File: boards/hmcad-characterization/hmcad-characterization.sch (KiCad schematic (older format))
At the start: 46 parts, among them J1 BARREL, J10 SMA, J11 SMA, J12 CONN_INTEGRALSTICK_FPGA_HOST, J2 SMA, J3 SMA, J4 SMA, J5 SMA, J6 SMA, J7 SMA, J8 SMA, J9 SMA, U1 ASG2-D-X-A-1000.000MHZ, U2 SIT9122AI-2D3-33E625.000000T, U3 PI6C59S6005, U4 LT3042, U5 HMCAD1520

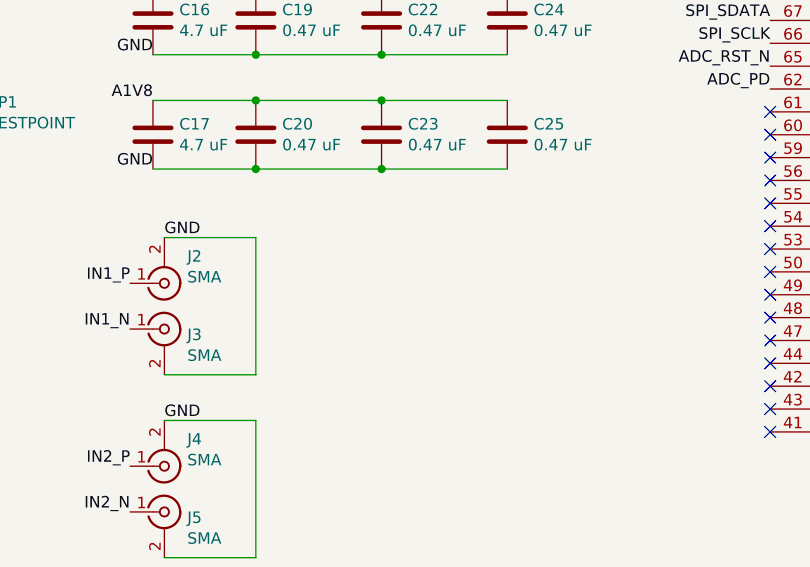
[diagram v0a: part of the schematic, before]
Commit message: finished schematic review on hmcad-characterization, ready to start layout
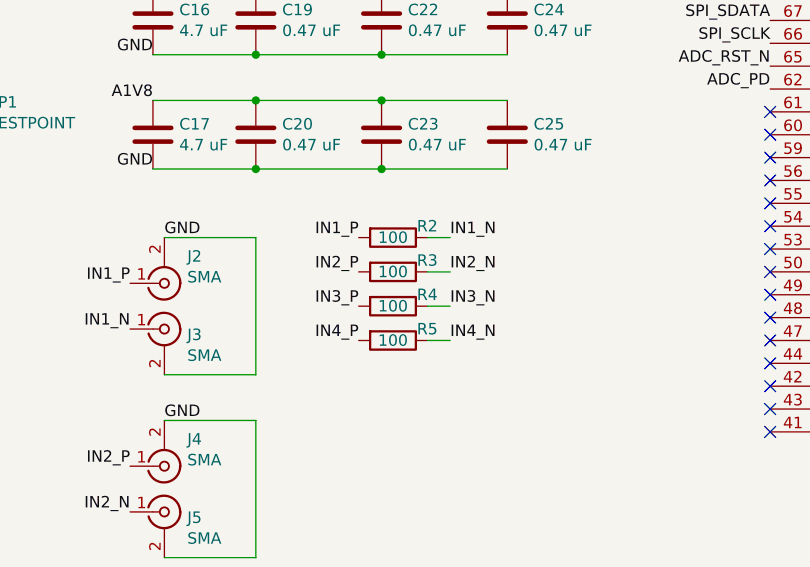
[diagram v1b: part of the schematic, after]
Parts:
- added R2, R3, R4, R5: 100, azonenberg_pcb:EIA_0402_RES_NOSILK, symbol device:R
- C1, C11, C12, C13, C14, C15, C18, C19, C2, C20, C21, C22, C23, C24, C25, C4, C5, C6, C7, C8, C9: footprint (none) -> azonenberg_pcb:EIA_0402_CAP_NOSILK
- C10, C16, C17, C3: footprint (none) -> azonenberg_pcb:EIA_0603_CAP_NOSILK
- F1, FB1: footprint (none) -> azonenberg_pcb:EIA_0603_INDUCTOR_NOSILK
- J1: footprint (none) -> azonenberg_pcb:CONN_CUI_PJ-058BH_HIPWR_BARREL_NOSLOT
- J10, J11, J2, J3, J4, J5, J6, J7, J8, J9: footprint (none) -> azonenberg_pcb:CONN_SMA_EDGE_SAMTEC_SMA_J_P_H_ST_EM1
- J12: footprint (none) -> azonenberg_pcb:CONN_SAMTEC_QSH-060-01-L-D-A
- R1: footprint (none) -> azonenberg_pcb:EIA_0402_RES_NOSILK
- TP1: footprint (none) -> azonenberg_pcb:TESTPOINT_SMT_0.5MM
- U1: footprint (none) -> azonenberg_pcb:OSCILLATOR_LVDS_2.5x2.0
- U2: footprint (none) -> azonenberg_pcb:OSCILLATOR_LVDS_7.0x5.0
- U3: footprint (none) -> azonenberg_pcb:QFN_24_0.5MM_4x4MM
- U4: footprint (none) -> azonenberg_pcb:DFN_10_0.5MM_3x3MM
- U5: footprint (none) -> azonenberg_pcb:QFN_48_0.5MM_7x7MM
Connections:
- net IN1_N: now also R2.1
- net IN1_P: now also R2.2
- net IN2_N: now also R3.1
- net IN2_P: now also R3.2
- net IN3_N: now also R4.1
- net IN3_P: now also R4.2
- net IN4_N: now also R5.1
- net IN4_P: now also R5.2

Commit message: Continued layout on ADC test board. Fixed a bunch of plane crossings.
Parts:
- added C26, C27: 4.7 uF, azonenberg_pcb:EIA_0603_CAP_NOSILK, symbol device:C
- added C28: 0.47 uF, azonenberg_pcb:EIA_0402_CAP_NOSILK, symbol device:C
- added U6: LT3042, azonenberg_pcb:DFN_10_0.5MM_3x3MM, symbol power-azonenberg:LT3042
- R1: value 33K 1% -> 9.09K 0.1%
- U1, U2: symbol osc-azonenberg:OSC_LVDS -> osc-azonenberg:OSC_LVDS_NOPAD
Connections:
- net 1V8: now also C28.1
- net 3V3: now also C28.2; no longer U4.6 (PGFB)
- net A1V8: now also C27.2, U6.10 (OUT), U6.9 (OUTS)
- net ADC_PD: now also J12.68 (IO_1V8); no longer J12.62 (IO_1V8)
- net ADC_RST_N: now also J12.66 (IO_1V8); no longer J12.65 (IO_1V8)
- net BUF_IN_SEL: now also J12.120 (IO_3V3); no longer J12.74 (IO_3V3)
- net BUF_MUXSEL: now also J12.116 (IO_3V3); no longer J12.73 (IO_3V3)
- net CLK_1GHZ_AC_N: now also C5.1; no longer C6.1
- net CLK_1GHZ_AC_P: now also C6.1; no longer C5.1
- net CLK_625MHZ_N: now also C7.2; no longer C8.2
- net CLK_625MHZ_P: now also C8.2; no longer C7.2
- net FCLK_N: now also J12.12 (LVDS_DQ8_P); no longer J12.10 (LVDS_DQ8_N)
- net FCLK_P: now also J12.10 (LVDS_DQ8_N); no longer J12.12 (LVDS_DQ8_P)
- net GND: now also U5.PAD (AVSS), C26.1, C27.1, U6.5 (ILIM), U6.8 (GND), U6.PAD (GND); no longer U1.PAD (GND), U2.PAD (GND)
- net LVDS_1A_N: now also J12.17 (LVDS_DQ7_P); no longer J12.34 (LVDS_DQ0_N)
- net LVDS_1A_P: now also J12.15 (LVDS_DQ7_N); no longer J12.36 (LVDS_DQ0_P)
- net LVDS_1B_N: now also J12.23 (LVDS_DQ5_P); no longer J12.33 (LVDS_DQ1_N)
- net LVDS_1B_P: now also J12.21 (LVDS_DQ5_N); no longer J12.35 (LVDS_DQ1_P)
- net LVDS_2A_N: now also J12.29 (LVDS_DQ3_P); no longer J12.28 (LVDS_DQ2_N)
- net LVDS_2A_P: now also J12.27 (LVDS_DQ3_N); no longer J12.30 (LVDS_DQ2_P)
- net LVDS_2B_N: now also J12.35 (LVDS_DQ1_P); no longer J12.27 (LVDS_DQ3_N)
- net LVDS_2B_P: now also J12.33 (LVDS_DQ1_N); no longer J12.29 (LVDS_DQ3_P)
- net LVDS_3A_N: now also J12.18 (LVDS_DQ6_P); no longer J12.22 (LVDS_DQ4_N)
- net LVDS_3A_P: now also J12.16 (LVDS_DQ6_N); no longer J12.24 (LVDS_DQ4_P)
- net LVDS_3B_N: now also J12.24 (LVDS_DQ4_P); no longer J12.21 (LVDS_DQ5_N)
- net LVDS_3B_P: now also J12.22 (LVDS_DQ4_N); no longer J12.23 (LVDS_DQ5_P)
- net LVDS_4A_N: now also J12.30 (LVDS_DQ2_P); no longer J12.16 (LVDS_DQ6_N)
- net LVDS_4A_P: now also J12.28 (LVDS_DQ2_N); no longer J12.18 (LVDS_DQ6_P)
- net LVDS_4B_N: now also J12.36 (LVDS_DQ0_P); no longer J12.15 (LVDS_DQ7_N)
- net LVDS_4B_P: now also J12.34 (LVDS_DQ0_N); no longer J12.17 (LVDS_DQ7_P)
- net SPI_CS_N: now also J12.61 (IO_1V8); no longer J12.68 (IO_1V8)
- net SPI_SCLK: now also J12.67 (IO_1V8); no longer J12.66 (IO_1V8)
- net SPI_SDATA: now also J12.65 (IO_1V8); no longer J12.67 (IO_1V8)
- net DEBUG_AC_P: now reaches C13.2, U3.10 (Q4_P)
- net DEBUG_AC_N: now reaches C14.2, U3.11 (Q4_N)
- net ADC_AC_P: now reaches C11.2, U3.23 (Q0_P)
- net ADC_AC_N: now reaches C12.2, U3.24 (Q0_N)
- net 3V3_1: now reaches C3.2, FB1.1, U4.1 (IN), U4.2 (IN), U4.3 (EN/UV)
- net 3V3_1: now also U4.6 (PGFB), C26.2, U6.1 (IN), U6.2 (IN), U6.3 (EN/UV), U6.6 (PGFB)
- net RSET: now reaches R1.1, U4.7 (SET)
- net RSET: now also U6.7 (SET)
- no-connect marks 55 -> 56
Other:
- note added: "Polarity inverted on all signals\nfor routability"
- note added: "Ref plane changing for LCLK"
- moved on the sheet: C10, C11, C12, C13, C14, C3, C7, C8, FB1, J10, J11, R1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
